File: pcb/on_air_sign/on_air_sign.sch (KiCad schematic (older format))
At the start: 26 parts, among them J1 USB_B, J2 ICSP, Q1 PN2222A, Q2 PN2222A, Q3 PN2222A, U1 AMS1117-3.3, U2 ATmega328P-AU, U3 CH340G, U4 NRF24L01_Breakout, Y1 12MHz, Y2 8MHz

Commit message: assign footprints
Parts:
- removed C4: C, symbol Device:C
- added C3, C7: 100n, Capacitor_THT:C_Rect_L7.0mm_W2.5mm_P5.00mm, symbol Device:C
- added C5: 47u, Capacitor_THT:CP_Radial_D5.0mm_P2.50mm, symbol Device:C
- C1: value C -> 47u; footprint (none) -> Capacitor_THT:CP_Radial_D5.0mm_P2.50mm
- C10: renamed from C6; footprint (none) -> Capacitor_THT:C_Rect_L7.0mm_W2.5mm_P5.00mm
- C11: renamed from C7; footprint (none) -> Capacitor_THT:C_Rect_L7.0mm_W2.5mm_P5.00mm
- C12: renamed from C8; footprint (none) -> Capacitor_THT:C_Rect_L7.0mm_W2.5mm_P5.00mm
- C2: footprint (none) -> Capacitor_THT:C_Rect_L7.0mm_W2.5mm_P5.00mm
- C4: renamed from C3; footprint (none) -> Capacitor_THT:C_Rect_L7.0mm_W2.5mm_P5.00mm
- C6: renamed from C5; footprint (none) -> Capacitor_THT:C_Rect_L7.0mm_W3.5mm_P5.00mm
- C8: renamed from C9; footprint (none) -> Capacitor_THT:C_Rect_L7.0mm_W2.5mm_P5.00mm
- C9: renamed from C10; footprint (none) -> Capacitor_THT:C_Rect_L7.0mm_W2.5mm_P5.00mm
- J1: footprint (none) -> Connector_USB:USB_B_OST_USB-B1HSxx_Horizontal
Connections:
- net +3V3: now also C5.1, C7.1
- net GND: now also C3.1, C5.2, C7.2
- net at U2.20 (AREF): now also C3.2
- no-connect marks 21 -> 20

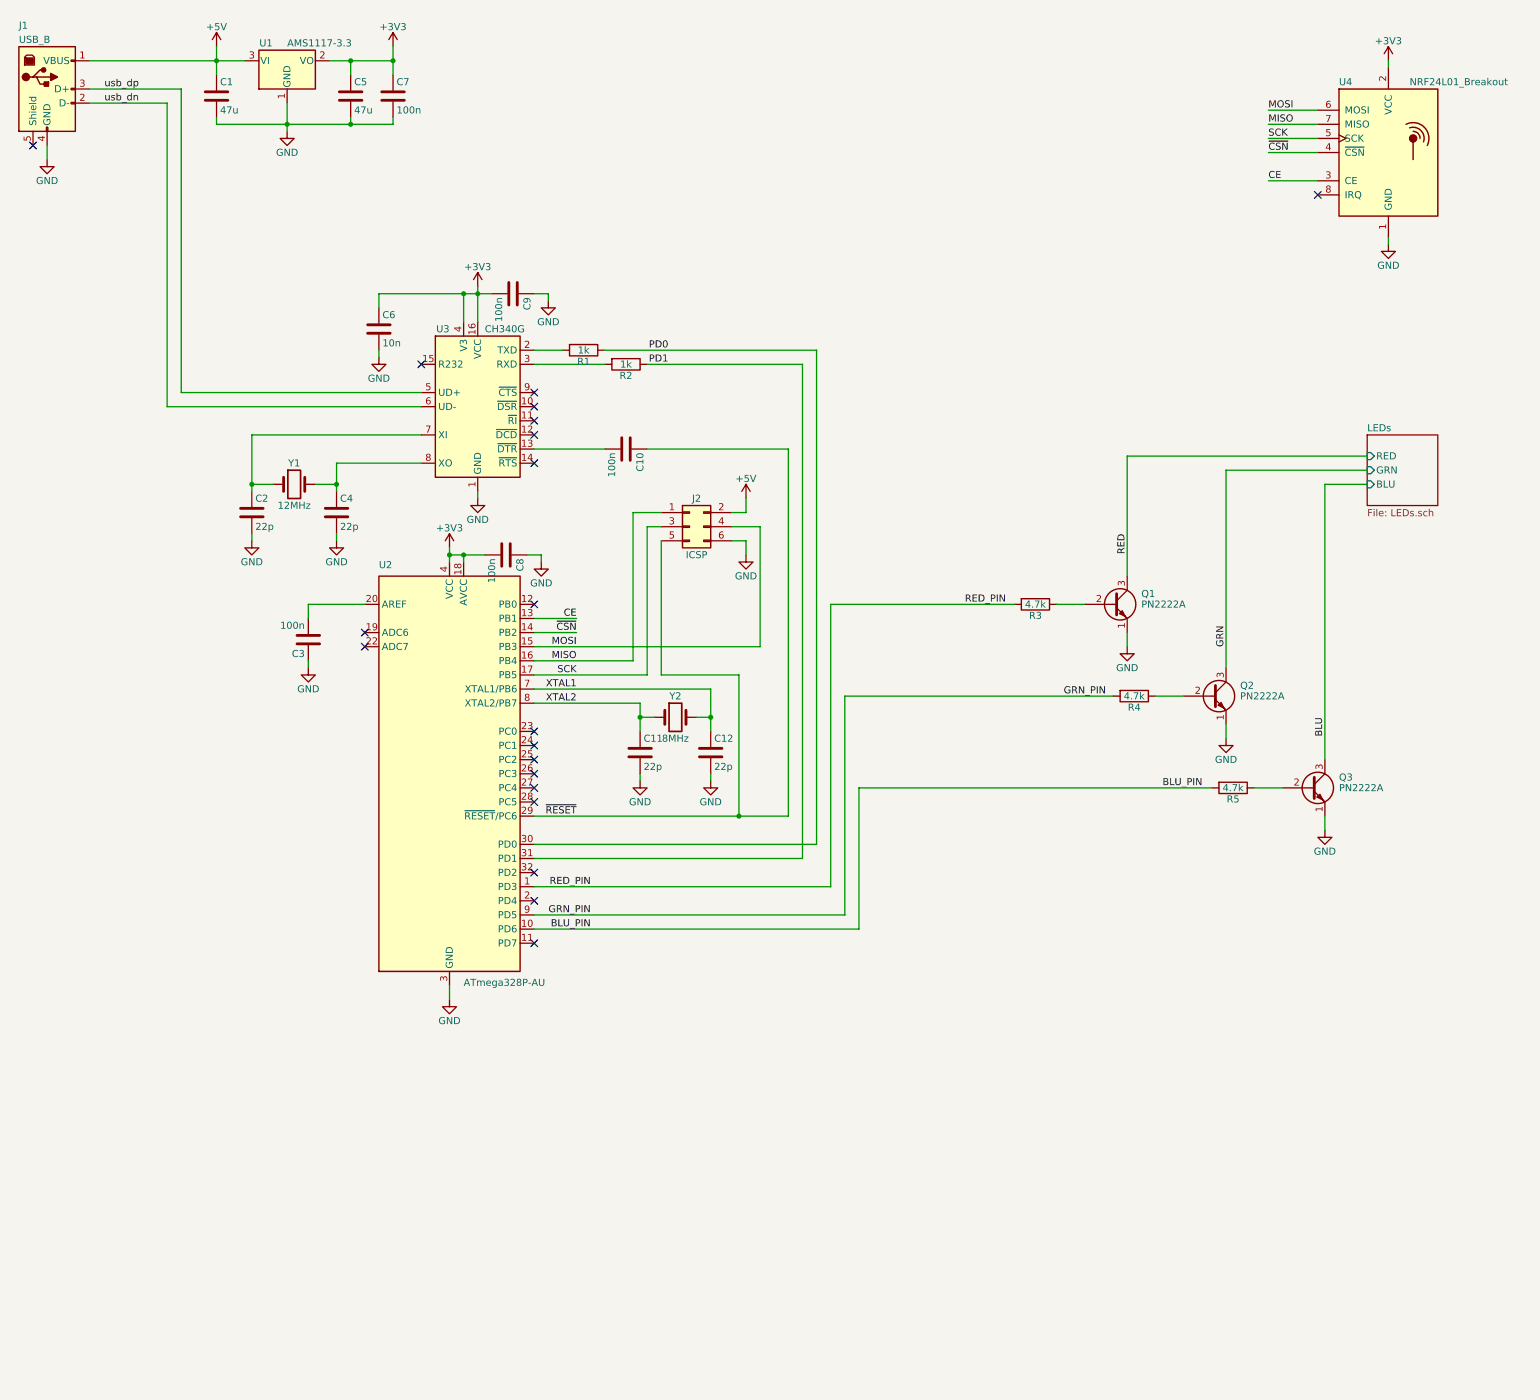
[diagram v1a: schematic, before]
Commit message: simplify schematic
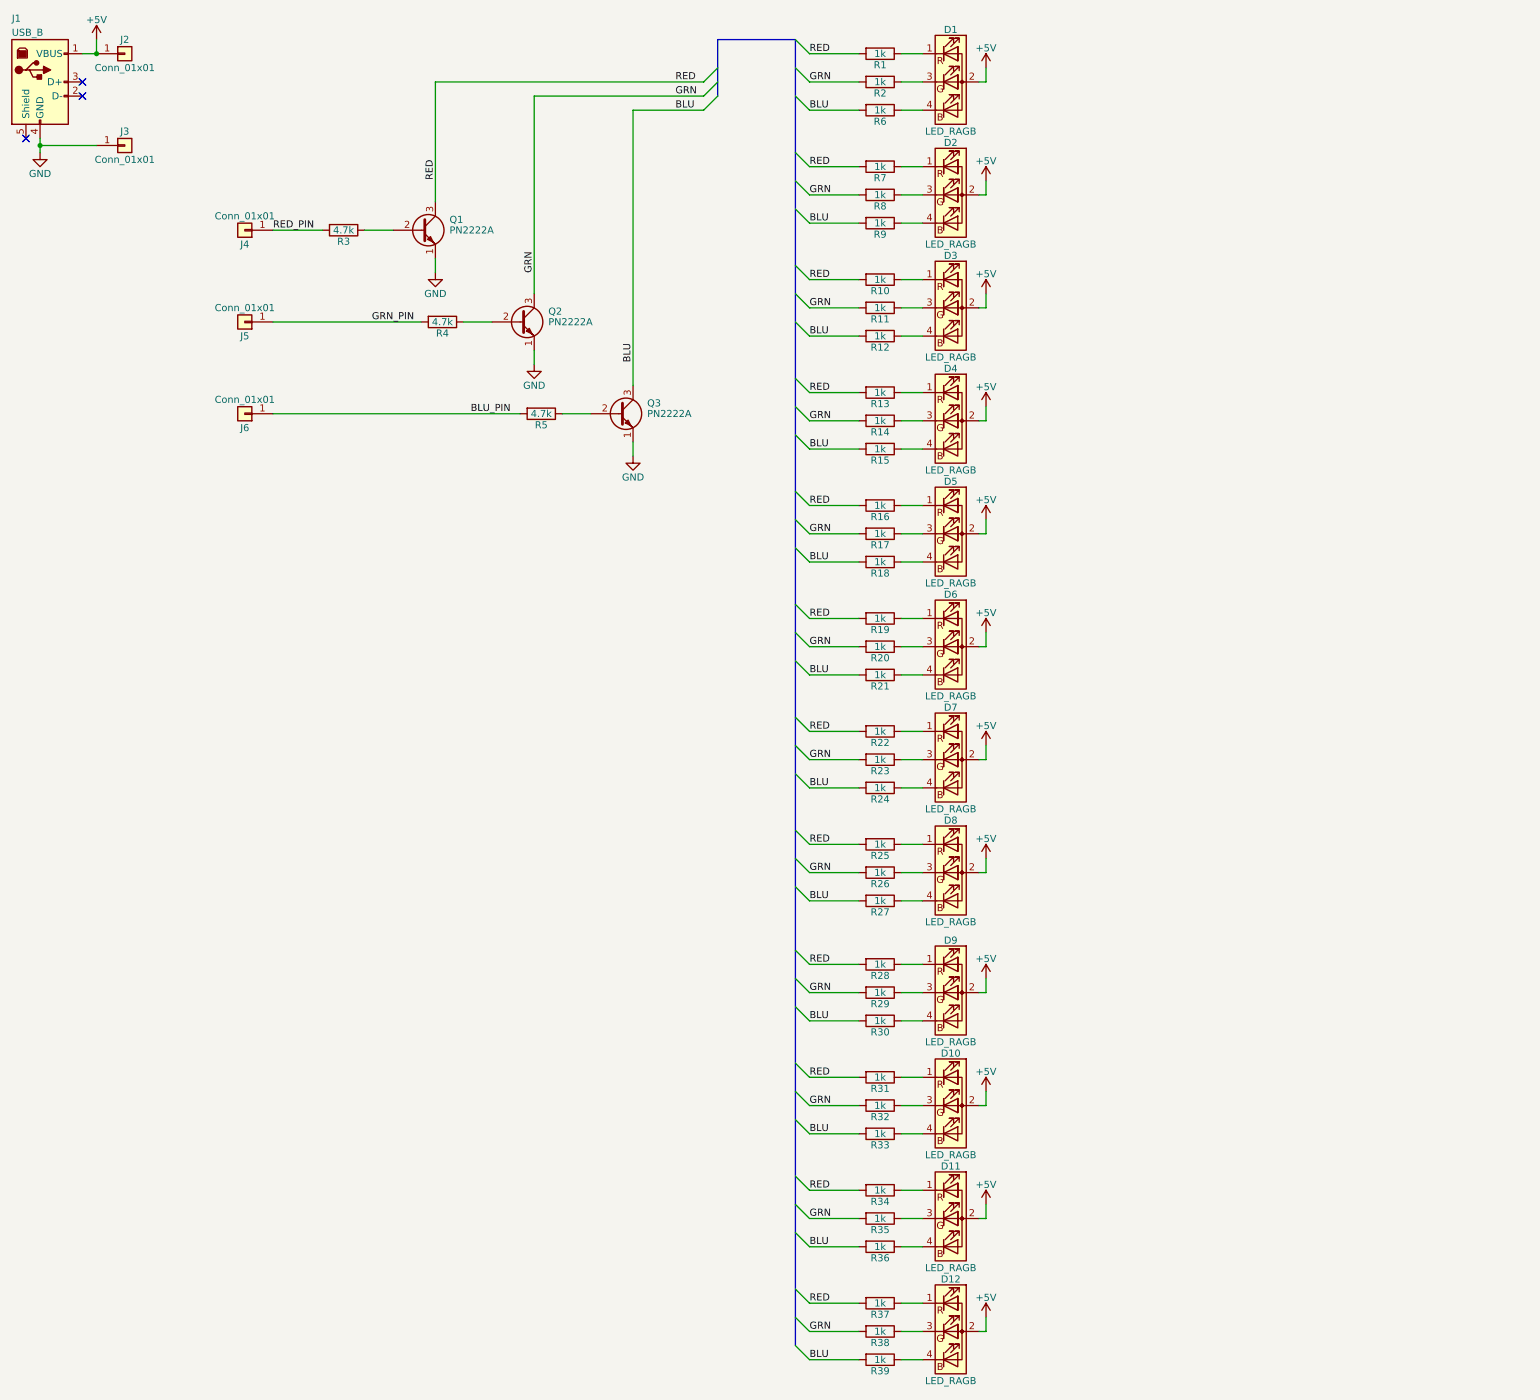
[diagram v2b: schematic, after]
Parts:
- removed C1, C5: 47u, Capacitor_THT:CP_Radial_D5.0mm_P2.50mm, symbol Device:C
- removed C10, C3, C7, C8, C9: 100n, Capacitor_THT:C_Rect_L7.0mm_W2.5mm_P5.00mm, symbol Device:C
- removed C11, C12, C2, C4: 22p, Capacitor_THT:C_Rect_L7.0mm_W2.5mm_P5.00mm, symbol Device:C
- removed C6: 10n, Capacitor_THT:C_Rect_L7.0mm_W3.5mm_P5.00mm, symbol Device:C
- removed J2: ICSP, Connector_PinSocket_2.54mm:PinSocket_2x03_P2.54mm_Vertical, symbol Connector_Generic:Conn_02x03_Odd_Even
- removed U1: AMS1117-3.3, Package_TO_SOT_SMD:SOT-223-3_TabPin2, symbol Regulator_Linear:AMS1117-3.3
- removed U2: ATmega328P-AU, Package_QFP:TQFP-32_7x7mm_P0.8mm, symbol MCU_Microchip_ATmega:ATmega328P-AU
- removed U3: CH340G, Package_SO:SOIC-16_3.9x9.9mm_P1.27mm, symbol Interface_USB:CH340G
- removed U4: NRF24L01_Breakout, RF_Module:nRF24L01_Breakout, symbol RF:NRF24L01_Breakout
- removed Y1: 12MHz, Crystal:Crystal_HC18-U_Vertical, symbol Device:Crystal
- removed Y2: 8MHz, Crystal:Crystal_HC18-U_Vertical, symbol Device:Crystal
- added D1, D10, D11, D12, D2, D3, D4, D5, D6, D7, D8, D9: LED_RAGB, LED_THT:LED_D5.0mm-4_RGB_Staggered_Pins, symbol Device:LED_RAGB
- added J2, J3, J4, J5, J6: Conn_01x01, TestPoint:TestPoint_Pad_2.5x2.5mm, symbol Connector_Generic:Conn_01x01
- added R10, R11, R12, R13, R14, R15, R16, R17, R18, R19, R20, R21, R22, R23, R24, R25, R26, R27, R28, R29, R30, R31, R32, R33, R34, R35, R36, R37, R38, R39, R6, R7, R8, R9: 1k, Resistor_THT:R_Axial_DIN0204_L3.6mm_D1.6mm_P7.62mm_Horizontal, symbol Device:R
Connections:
- net +5V: now also D1.2 (A), D10.2 (A), D11.2 (A), D12.2 (A), D2.2 (A), D3.2 (A), D4.2 (A), D5.2 (A), D6.2 (A), D7.2 (A), D8.2 (A), D9.2 (A), J2.1 (Pin_1)
- net BLU: now also R12.2, R15.2, R18.2, R21.2, R24.2, R27.2, R30.2, R33.2, R36.2, R39.2, R6.2, R9.2
- net BLU_PIN: now also J6.1 (Pin_1)
- net GND: now also J3.1 (Pin_1)
- net GRN: now also R2.2, R11.2, R14.2, R17.2, R20.2, R23.2, R26.2, R29.2, R32.2, R35.2, R38.2, R8.2
- net GRN_PIN: now also J5.1 (Pin_1)
- net RED: now also R1.2, R10.2, R13.2, R16.2, R19.2, R22.2, R25.2, R28.2, R31.2, R34.2, R37.2, R7.2
- net RED_PIN: now also J4.1 (Pin_1)
- net PD0: no longer names the net of R1.1
- net PD0: now also D1.1 (RK)
- net PD1: no longer names the net of R2.1
- net PD1: now also D1.3 (GK)
- net usb_dn: no longer names the net of J1.2 (D-)
- net usb_dp: no longer names the net of J1.3 (D+)
- new net: D5.1 (RK), R16.1
- new net: D5.3 (GK), R17.1
- new net: D5.4 (BK), R18.1
- new net: D6.1 (RK), R19.1
- new net: D6.3 (GK), R20.1
- new net: D6.4 (BK), R21.1
- new net: D7.1 (RK), R22.1
- new net: D7.3 (GK), R23.1
- new net: D7.4 (BK), R24.1
- new net: D8.1 (RK), R25.1
- new net: D8.3 (GK), R26.1
- new net: D8.4 (BK), R27.1
- new net: D1.4 (BK), R6.1
- new net: D2.1 (RK), R7.1
- new net: D2.3 (GK), R8.1
- new net: D2.4 (BK), R9.1
- new net: D3.1 (RK), R10.1
- new net: D3.3 (GK), R11.1
- new net: D3.4 (BK), R12.1
- new net: D4.1 (RK), R13.1
- new net: D4.3 (GK), R14.1
- new net: D4.4 (BK), R15.1
- new net: D12.4 (BK), R39.1
- new net: D12.3 (GK), R38.1
- new net: D12.1 (RK), R37.1
- new net: D11.4 (BK), R36.1
- new net: D11.3 (GK), R35.1
- new net: D11.1 (RK), R34.1
- new net: D10.4 (BK), R33.1
- new net: D10.3 (GK), R32.1
- new net: D10.1 (RK), R31.1
- new net: D9.4 (BK), R30.1
- new net: D9.3 (GK), R29.1
- new net: D9.1 (RK), R28.1
- no-connect marks 20 -> 3
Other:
- moved on the sheet: J1, Q1, Q2, Q3, R3, R4, R5

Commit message: update schema and board shape
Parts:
- removed J2, J3: Conn_01x01, TestPoint:TestPoint_Pad_2.5x2.5mm, symbol Connector_Generic:Conn_01x01
- added C1, C2: 22p, Capacitor_THT:C_Disc_D3.8mm_W2.6mm_P2.50mm, symbol Device:C
- added C4: 10n, Capacitor_SMD:C_0603_1608Metric_Pad1.08x0.95mm_HandSolder, symbol Device:C
- added C5: 100n, Capacitor_THT:C_Disc_D4.3mm_W1.9mm_P5.00mm, symbol Device:C
- added J2: SERAIL, Connector_PinHeader_2.54mm:PinHeader_1x06_P2.54mm_Vertical, symbol Connector_Generic:Conn_01x06
- added R40, R41: 0, Resistor_SMD:R_0805_2012Metric_Pad1.20x1.40mm_HandSolder, symbol Device:R
- added U1: CH340G, Package_SO:SOIC-16_3.9x9.9mm_P1.27mm, symbol Interface_USB:CH340G
- added Y1: 12MHz, Crystal:Crystal_HC49-4H_Vertical, symbol Device:Crystal_Small
- J1: value USB_B -> USB_B_Micro; footprint Connector_USB:USB_B_OST_USB-B1HSxx_Horizontal -> Connector_USB:USB_Micro-B_GCT_USB3076-30-A; symbol Connector:USB_B -> Connector:USB_B_Micro
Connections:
- net GND: now also J1.5 (GND), J1.6 (Shield), C1.2, C2.2, C4.1, C5.1, J2.1 (Pin_1), U1.1 (GND); no longer J1.4 (GND)
- net at J1.2 (D-): now also R40.1
- net at J1.3 (D+): now also R41.1
- new net: C4.2, U1.4 (V3)
- new net: C1.1, U1.7 (XI), Y1.1
- new net: C2.1, U1.8 (XO), Y1.2
- new net +3V3: C5.2, J2.3 (Pin_3), U1.16 (VCC)
- new net D+: R41.2, U1.5 (UD+)
- new net D-: R40.2, U1.6 (UD-)
- new net RXD: J2.5 (Pin_5), U1.3 (RXD)
- new net TDX: J2.4 (Pin_4), U1.2 (TXD)
- new net ~CTS: J2.2 (Pin_2), U1.9 (~CTS)
- new net ~DTR: J2.6 (Pin_6), U1.13 (~DTR)
- no-connect marks 3 -> 6
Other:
- note added: "DUE TO SPACE CONSTRAINS HAND WIRING IS REQUIRED\nHAND WIRE ARDUINO PRO MINI CLONE TO PCB\nCONNECT TO SERIAL AND RGB PINS\nALSO CONNECT A NRF24L01 MODULE TO ARDUINO"
- moved on the sheet: D1, D10, D11, D12, D2, D3, D4, D5, D6, D7, D8, D9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
